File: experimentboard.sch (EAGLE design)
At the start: 173 parts, among them IC1 TL072P, IC2 LM317, IC3 LM337, IC4 TL072P, IC5 TL072P, IC6 TL072P, P1 PLR135/T9, P9 P9, U1 PCM1690, U2 DIR9001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

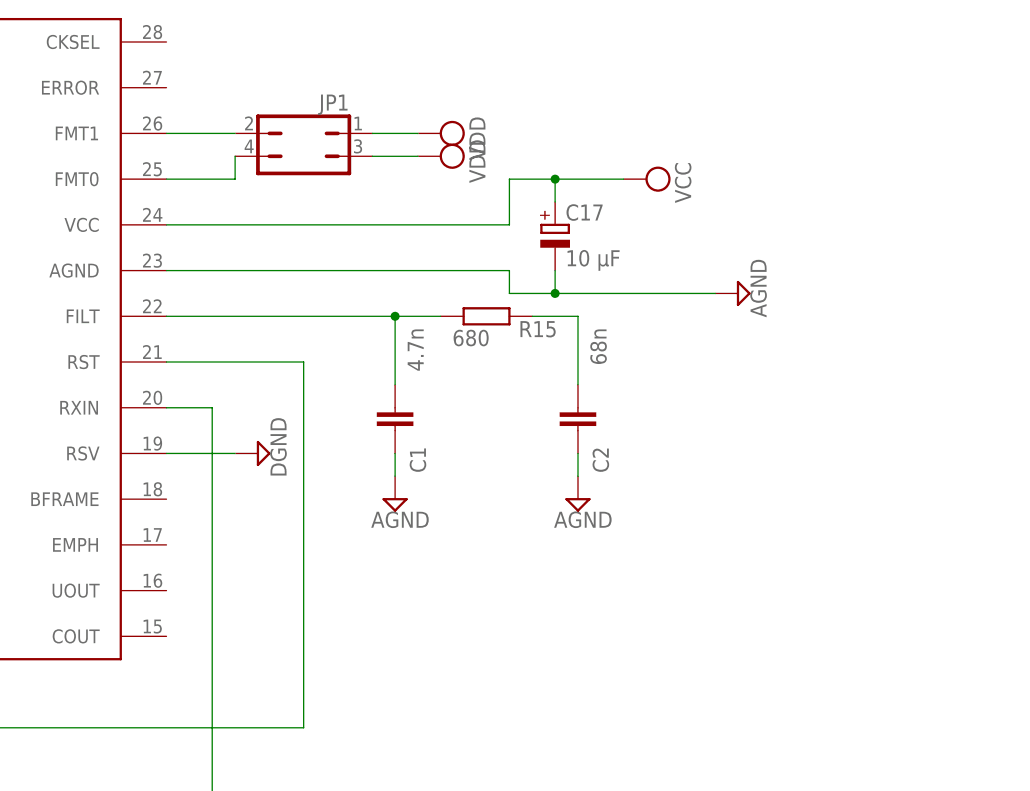
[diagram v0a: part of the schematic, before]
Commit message: Fixed DIR9001 VCC 3.3V misunderstanding
VCC is actually 3.3V, and AGND is only different from GND in where the
FILT ties. Almost have that complete. Need to tie the AGND to DGND
first, and not at a common point with the filter.
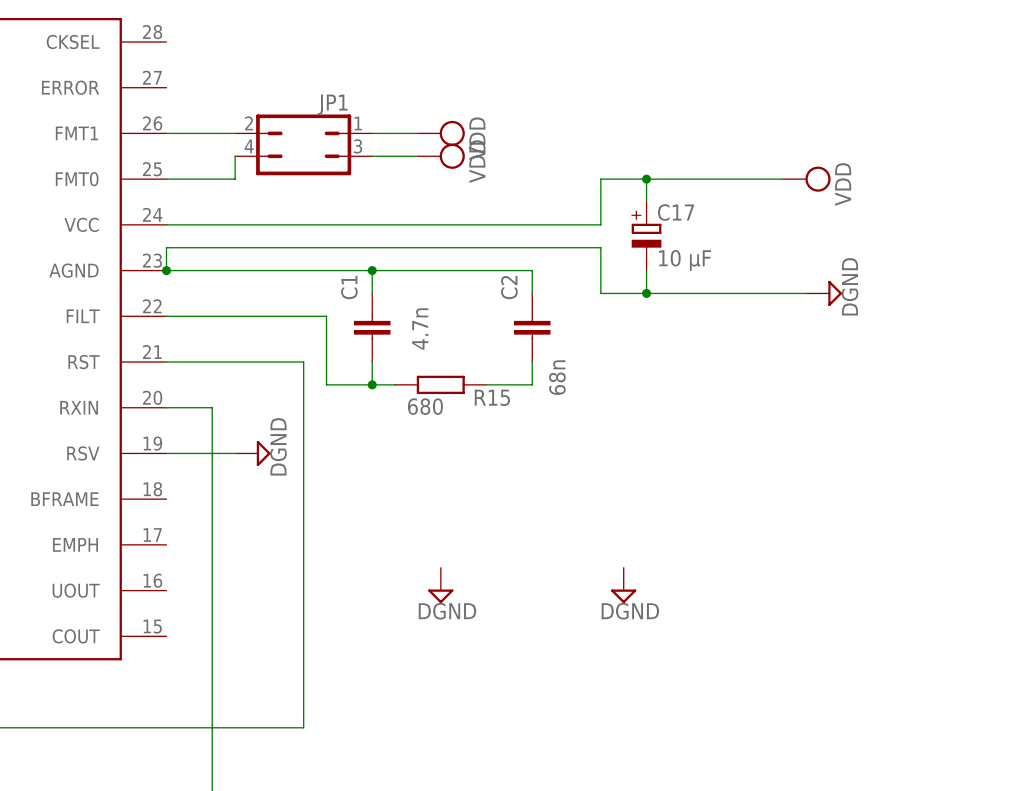
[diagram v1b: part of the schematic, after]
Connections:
- net N$4 renamed FILT
- net AGND: no longer C1.1, C17.-, C2.1, U2.AGND
- net DGND: now also C1.1, C17.-, C2.1, U2.AGND
- net VCC: no longer C17.+, U2.VCC
- net VDD: now also C17.+, U2.VCC
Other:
- moved on the sheet: C1, C17, C2, R15
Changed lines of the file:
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@@
 <part name="SUPPLY1" library="supply2" deviceset="DGND" device=""/>
 <part name="SUPPLY2" library="supply2" deviceset="VDD" device=""/>
-<part name="SUPPLY4" library="supply2" deviceset="VCC" device=""/>
-<part name="SUPPLY10" library="supply2" deviceset="AGND" device=""/>
 <part name="C1" library="rcl" deviceset="C-EU" device="050-024X044" value="4.7n"/>
 <part name="C2" library="rcl" deviceset="C-EU" device="050-024X044" value="68n"/>
 <part name="R15" library="rcl" deviceset="R-EU_" device="0207/7" value="680"/>
-<part name="SUPPLY11" library="supply2" deviceset="AGND" device=""/>
-<part name="SUPPLY12" library="supply2" deviceset="AGND" device=""/>
 <part name="C15" library="rcl" deviceset="C-EU" device="050-024X044" value="1µF ml"/>
 <part name="JP1" library="jumper" deviceset="JP2Q" device=""/>
@@
 <part name="C17" library="rcl" deviceset="CPOL-EU" device="E2-5" value="10 µF"/>
 <part name="JP4" library="jumper" deviceset="JP1Q" device=""/>
+<part name="SUPPLY4" library="supply2" deviceset="VDD" device=""/>
+<part name="SUPPLY10" library="supply2" deviceset="DGND" device=""/>
+<part name="SUPPLY11" library="supply2" deviceset="DGND" device=""/>
+<part name="SUPPLY12" library="supply2" deviceset="DGND" device=""/>
 </parts>
 <sheets>
@@
 <instance part="SUPPLY1" gate="G$1" x="53.34" y="-91.44" rot="R270"/>
 <instance part="SUPPLY2" gate="G$1" x="53.34" y="-78.74" rot="R90"/>
-<instance part="SUPPLY4" gate="G$1" x="175.26" y="-78.74" rot="R270"/>
-<instance part="SUPPLY10" gate="G$1" x="185.42" y="-91.44" rot="R90"/>
-<instance part="C1" gate="G$1" x="147.32" y="-106.68" smashed="yes" rot="R180">
-<attribute name="NAME" x="148.971" y="-108.458" size="1.778" layer="95" rot="R270"/>
-<attribute name="VALUE" x="148.717" y="-95.25" size="1.778" layer="96" rot="R270"/>
-</instance>
-<instance part="C2" gate="G$1" x="167.64" y="-106.68" smashed="yes" rot="R180">
-<attribute name="NAME" x="169.291" y="-108.458" size="1.778" layer="95" rot="R270"/>
-<attribute name="VALUE" x="169.037" y="-95.25" size="1.778" layer="96" rot="R270"/>
-</instance>
-<instance part="R15" gate="G$1" x="157.48" y="-93.98" smashed="yes">
-<attribute name="NAME" x="161.036" y="-96.2914" size="1.778" layer="95"/>
-<attribute name="VALUE" x="153.67" y="-97.282" size="1.778" layer="96"/>
-</instance>
-<instance part="SUPPLY11" gate="G$1" x="147.32" y="-114.3"/>
-<instance part="SUPPLY12" gate="G$1" x="167.64" y="-114.3"/>
+<instance part="C1" gate="G$1" x="144.78" y="-93.98" smashed="yes">
+<attribute name="NAME" x="143.129" y="-92.202" size="1.778" layer="95" rot="R90"/>
+<attribute name="VALUE" x="151.003" y="-97.79" size="1.778" layer="96" rot="R90"/>
+</instance>
+<instance part="C2" gate="G$1" x="162.56" y="-93.98" smashed="yes">
+<attribute name="NAME" x="160.909" y="-92.202" size="1.778" layer="95" rot="R90"/>
+<attribute name="VALUE" x="166.243" y="-102.87" size="1.778" layer="96" rot="R90"/>
+</instance>
+<instance part="R15" gate="G$1" x="152.4" y="-101.6" smashed="yes">
+<attribute name="NAME" x="155.956" y="-103.9114" size="1.778" layer="95"/>
+<attribute name="VALUE" x="148.59" y="-104.902" size="1.778" layer="96"/>
+</instance>
 <instance part="C15" gate="G$1" x="58.42" y="-83.82" smashed="yes">
 <attribute name="NAME" x="62.484" y="-82.423" size="1.778" layer="95"/>
@@
 <instance part="JP3" gate="A" x="198.12" y="241.3" rot="R90"/>
 <instance part="C16" gate="G$1" x="96.52" y="-187.96" rot="R90"/>
-<instance part="C17" gate="G$1" x="165.1" y="-83.82"/>
+<instance part="C17" gate="G$1" x="175.26" y="-83.82"/>
 <instance part="JP4" gate="A" x="124.46" y="215.9" rot="R90"/>
+<instance part="SUPPLY4" gate="G$1" x="193.04" y="-78.74" rot="R270"/>
+<instance part="SUPPLY10" gate="G$1" x="195.58" y="-91.44" rot="R90"/>
+<instance part="SUPPLY11" gate="G$1" x="152.4" y="-124.46"/>
+<instance part="SUPPLY12" gate="G$1" x="172.72" y="-124.46"/>
 </instances>
 <busses>
@@
 <pinref part="R9" gate="G$1" pin="2"/>
 <wire x1="-93.98" y1="22.86" x2="-93.98" y2="17.78" width="0.1524" layer="91"/>
+</segment>
+<segment>
+<pinref part="U2" gate="G$1" pin="VCC"/>
+<wire x1="121.92" y1="-83.82" x2="170.18" y2="-83.82" width="0.1524" layer="91"/>
+<wire x1="170.18" y1="-83.82" x2="170.18" y2="-78.74" width="0.1524" layer="91"/>
+<wire x1="170.18" y1="-78.74" x2="175.26" y2="-78.74" width="0.1524" layer="91"/>
+<pinref part="C17" gate="G$1" pin="+"/>
+<wire x1="175.26" y1="-81.28" x2="175.26" y2="-78.74" width="0.1524" layer="91"/>
+<junction x="175.26" y="-78.74"/>
+<pinref part="SUPPLY4" gate="G$1" pin="VDD"/>
+<wire x1="175.26" y1="-78.74" x2="190.5" y2="-78.74" width="0.1524" layer="91"/>
 </segment>
 </net>
@@
 <wire x1="-68.58" y1="-15.24" x2="-83.82" y2="-15.24" width="0.1524" layer="91"/>
 <junction x="-83.82" y="-15.24"/>
+</segment>
+<segment>
+<pinref part="SUPPLY10" gate="G$1" pin="DGND"/>
+<wire x1="193.04" y1="-91.44" x2="175.26" y2="-91.44" width="0.1524" layer="91"/>
+<pinref part="C17" gate="G$1" pin="-"/>
+<wire x1="175.26" y1="-88.9" x2="175.26" y2="-91.44" width="0.1524" layer="91"/>
+<junction x="175.26" y="-91.44"/>
+<wire x1="175.26" y1="-91.44" x2="170.18" y2="-91.44" width="0.1524" layer="91"/>
+<pinref part="U2" gate="G$1" pin="AGND"/>
+<wire x1="162.56" y1="-88.9" x2="144.78" y2="-88.9" width="0.1524" layer="91"/>
+<wire x1="144.78" y1="-88.9" x2="121.92" y2="-88.9" width="0.1524" layer="91"/>
+<pinref part="C1" gate="G$1" pin="1"/>
+<wire x1="144.78" y1="-91.44" x2="144.78" y2="-88.9" width="0.1524" layer="91"/>
+<junction x="144.78" y="-88.9"/>
+<pinref part="C2" gate="G$1" pin="1"/>
+<wire x1="162.56" y1="-91.44" x2="162.56" y2="-88.9" width="0.1524" layer="91"/>
+<wire x1="121.92" y1="-88.9" x2="121.92" y2="-86.36" width="0.1524" layer="91"/>
+<junction x="121.92" y="-88.9"/>
+<wire x1="121.92" y1="-86.36" x2="170.18" y2="-86.36" width="0.1524" layer="91"/>
+<wire x1="170.18" y1="-86.36" x2="170.18" y2="-91.44" width="0.1524" layer="91"/>
 </segment>
 </net>
@@
 </segment>
 <segment>
-<pinref part="SUPPLY10" gate="G$1" pin="AGND"/>
-<pinref part="U2" gate="G$1" pin="AGND"/>
-<wire x1="182.88" y1="-91.44" x2="165.1" y2="-91.44" width="0.1524" layer="91"/>
-<wire x1="165.1" y1="-91.44" x2="160.02" y2="-91.44" width="0.1524" layer="91"/>
-<wire x1="160.02" y1="-91.44" x2="160.02" y2="-88.9" width="0.1524" layer="91"/>
-<wire x1="160.02" y1="-88.9" x2="121.92" y2="-88.9" width="0.1524" layer="91"/>
-<pinref part="C17" gate="G$1" pin="-"/>
-<wire x1="165.1" y1="-88.9" x2="165.1" y2="-91.44" width="0.1524" layer="91"/>
-<junction x="165.1" y="-91.44"/>
-</segment>
-<segment>
-<pinref part="SUPPLY11" gate="G$1" pin="AGND"/>
-<pinref part="C1" gate="G$1" pin="1"/>
-<wire x1="147.32" y1="-111.76" x2="147.32" y2="-109.22" width="0.1524" layer="91"/>
-</segment>
-<segment>
-<pinref part="SUPPLY12" gate="G$1" pin="AGND"/>
-<pinref part="C2" gate="G$1" pin="1"/>
-<wire x1="167.64" y1="-111.76" x2="167.64" y2="-109.22" width="0.1524" layer="91"/>
-</segment>
-<segment>
 <pinref part="3_C5" gate="G$1" pin="1"/>
 <pinref part="SUPPLY30" gate="G$1" pin="AGND"/>
@@
 <pinref part="SUPPLY7" gate="G$1" pin="VCC"/>
 <wire x1="149.86" y1="-5.08" x2="177.8" y2="-5.08" width="0.1524" layer="91"/>
-</segment>
-<segment>
-<pinref part="U2" gate="G$1" pin="VCC"/>
-<pinref part="SUPPLY4" gate="G$1" pin="VCC"/>
-<wire x1="121.92" y1="-83.82" x2="160.02" y2="-83.82" width="0.1524" layer="91"/>
-<wire x1="160.02" y1="-83.82" x2="160.02" y2="-78.74" width="0.1524" layer="91"/>
-<wire x1="160.02" y1="-78.74" x2="165.1" y2="-78.74" width="0.1524" layer="91"/>
-<pinref part="C17" gate="G$1" pin="+"/>
-<wire x1="165.1" y1="-78.74" x2="172.72" y2="-78.74" width="0.1524" layer="91"/>
-<wire x1="165.1" y1="-81.28" x2="165.1" y2="-78.74" width="0.1524" layer="91"/>
-<junction x="165.1" y="-78.74"/>
 </segment>
 <segment>
@@
 </segment>
 </net>
-<net name="N$4" class="0">
+<net name="FILT" class="0">
 <segment>
 <pinref part="U2" gate="G$1" pin="FILT"/>
 <pinref part="R15" gate="G$1" pin="1"/>
-<wire x1="121.92" y1="-93.98" x2="147.32" y2="-93.98" width="0.1524" layer="91"/>
+<wire x1="121.92" y1="-93.98" x2="139.7" y2="-93.98" width="0.1524" layer="91"/>
+<wire x1="139.7" y1="-93.98" x2="139.7" y2="-101.6" width="0.1524" layer="91"/>
+<wire x1="139.7" y1="-101.6" x2="144.78" y2="-101.6" width="0.1524" layer="91"/>
 <pinref part="C1" gate="G$1" pin="2"/>
-<wire x1="147.32" y1="-93.98" x2="152.4" y2="-93.98" width="0.1524" layer="91"/>
-<wire x1="147.32" y1="-101.6" x2="147.32" y2="-93.98" width="0.1524" layer="91"/>
-<junction x="147.32" y="-93.98"/>
+<wire x1="144.78" y1="-101.6" x2="147.32" y2="-101.6" width="0.1524" layer="91"/>
+<wire x1="144.78" y1="-99.06" x2="144.78" y2="-101.6" width="0.1524" layer="91"/>
+<junction x="144.78" y="-101.6"/>
 </segment>
 </net>
@@
 <pinref part="R15" gate="G$1" pin="2"/>
 <pinref part="C2" gate="G$1" pin="2"/>
-<wire x1="162.56" y1="-93.98" x2="167.64" y2="-93.98" width="0.1524" layer="91"/>
-<wire x1="167.64" y1="-93.98" x2="167.64" y2="-101.6" width="0.1524" layer="91"/>
-</segment>
-</net>
+<wire x1="157.48" y1="-101.6" x2="162.56" y2="-101.6" width="0.1524" layer="91"/>
+<wire x1="162.56" y1="-101.6" x2="162.56" y2="-99.06" width="0.1524" layer="91"/>
+</segment>
+</net>

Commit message: Removed unnecessary decoupling cap
I had added it to decouple VCC to DIR9001, but it didn't even need VCC,
that was a bug.
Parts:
- removed C17: 10 µF, rcl:CPOL-EUE2-5
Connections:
- net DGND: no longer C17.-
- net VDD: no longer C17.+
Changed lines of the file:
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@@
 <part name="JP3" library="jumper" deviceset="JP1Q" device=""/>
 <part name="C16" library="rcl" deviceset="CPOL-EU" device="E2-5" value="10 µF"/>
-<part name="C17" library="rcl" deviceset="CPOL-EU" device="E2-5" value="10 µF"/>
 <part name="JP4" library="jumper" deviceset="JP1Q" device=""/>
 <part name="SUPPLY4" library="supply2" deviceset="VDD" device=""/>
@@
 <instance part="JP3" gate="A" x="198.12" y="241.3" rot="R90"/>
 <instance part="C16" gate="G$1" x="96.52" y="-187.96" rot="R90"/>
-<instance part="C17" gate="G$1" x="175.26" y="-83.82"/>
 <instance part="JP4" gate="A" x="124.46" y="215.9" rot="R90"/>
 <instance part="SUPPLY4" gate="G$1" x="193.04" y="-78.74" rot="R270"/>
@@
 <wire x1="121.92" y1="-83.82" x2="170.18" y2="-83.82" width="0.1524" layer="91"/>
 <wire x1="170.18" y1="-83.82" x2="170.18" y2="-78.74" width="0.1524" layer="91"/>
-<wire x1="170.18" y1="-78.74" x2="175.26" y2="-78.74" width="0.1524" layer="91"/>
-<pinref part="C17" gate="G$1" pin="+"/>
-<wire x1="175.26" y1="-81.28" x2="175.26" y2="-78.74" width="0.1524" layer="91"/>
-<junction x="175.26" y="-78.74"/>
 <pinref part="SUPPLY4" gate="G$1" pin="VDD"/>
-<wire x1="175.26" y1="-78.74" x2="190.5" y2="-78.74" width="0.1524" layer="91"/>
+<wire x1="170.18" y1="-78.74" x2="190.5" y2="-78.74" width="0.1524" layer="91"/>
 </segment>
 </net>
@@
 <segment>
 <pinref part="SUPPLY10" gate="G$1" pin="DGND"/>
-<wire x1="193.04" y1="-91.44" x2="175.26" y2="-91.44" width="0.1524" layer="91"/>
-<pinref part="C17" gate="G$1" pin="-"/>
-<wire x1="175.26" y1="-88.9" x2="175.26" y2="-91.44" width="0.1524" layer="91"/>
-<junction x="175.26" y="-91.44"/>
-<wire x1="175.26" y1="-91.44" x2="170.18" y2="-91.44" width="0.1524" layer="91"/>
+<wire x1="193.04" y1="-91.44" x2="170.18" y2="-91.44" width="0.1524" layer="91"/>
 <pinref part="U2" gate="G$1" pin="AGND"/>
 <wire x1="162.56" y1="-88.9" x2="144.78" y2="-88.9" width="0.1524" layer="91"/>
